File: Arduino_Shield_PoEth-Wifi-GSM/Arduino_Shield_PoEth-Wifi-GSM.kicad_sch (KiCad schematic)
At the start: 0 parts

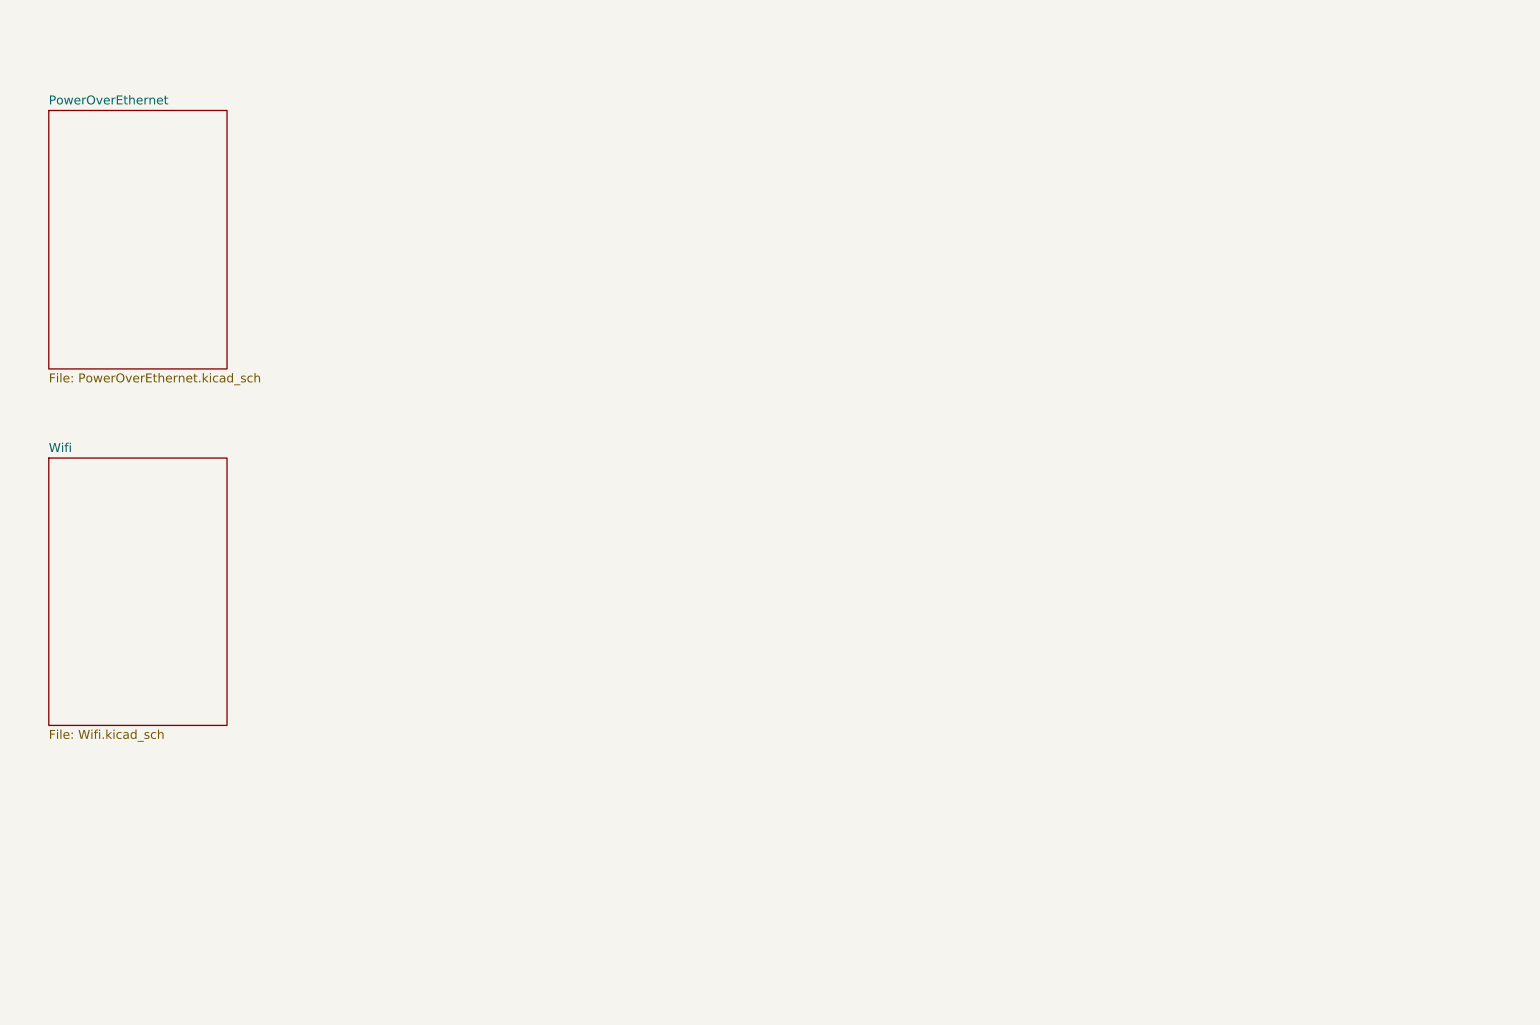
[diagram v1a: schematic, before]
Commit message: Tuning serial and crystal tracks
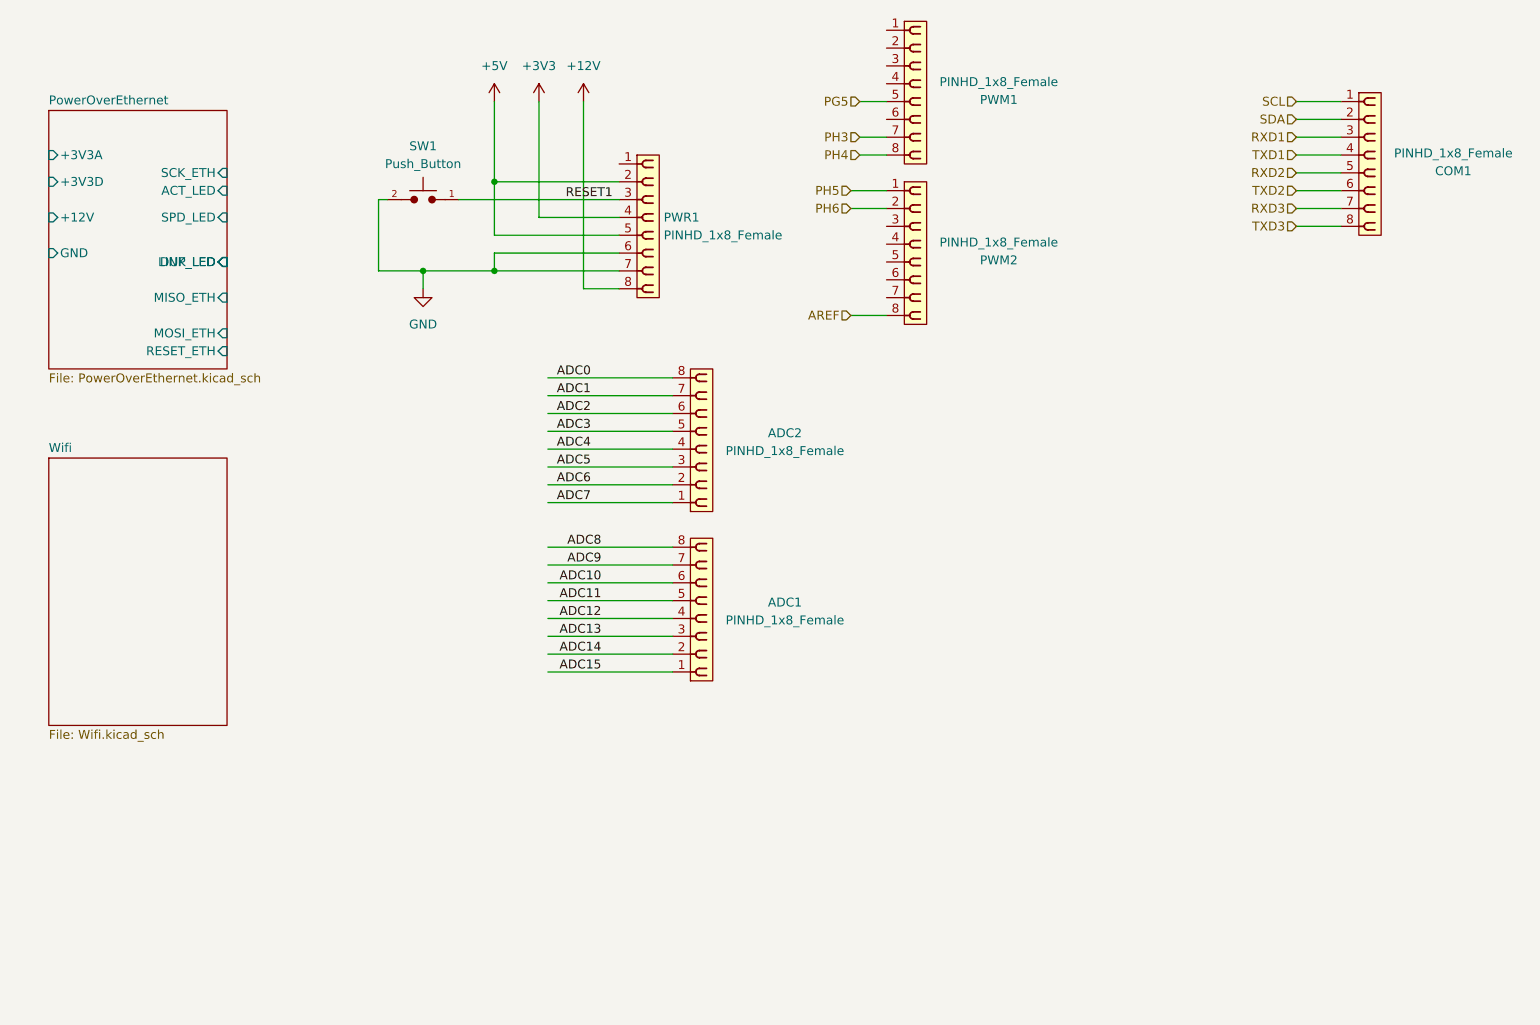
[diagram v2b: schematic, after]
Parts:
- added ADC1, ADC2, COM1, PWM1, PWM2, PWR1: PINHD_1x8_Female, Connector_PinSocket_2.54mm:PinSocket_1x08_P2.54mm_Vertical, symbol PCM_SL_Pin_Headers:PINHD_1x8_Female
- added SW1: Push_Button, Button_Switch_THT:SW_PUSH_6mm, symbol PCM_SL_Devices:Push_Button
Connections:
- new net +12V: PWR1.8
- new net +3V3: PWR1.4
- new net +5V: PWR1.2, PWR1.5
- new net ADC0: ADC2.8
- new net ADC1: ADC2.7
- new net ADC10: ADC1.6
- new net ADC11: ADC1.5
- new net ADC12: ADC1.4
- new net ADC13: ADC1.3
- new net ADC14: ADC1.2
- new net ADC15: ADC1.1
- new net ADC2: ADC2.6
- new net ADC3: ADC2.5
- new net ADC4: ADC2.4
- new net ADC5: ADC2.3
- new net ADC6: ADC2.2
- new net ADC7: ADC2.1
- new net ADC8: ADC1.8
- new net ADC9: ADC1.7
- new net AREF: PWM2.8
- new net GND: PWR1.6, PWR1.7, SW1.2
- new net PG5: PWM1.5
- new net PH3: PWM1.7
- new net PH4: PWM1.8
- new net PH5: PWM2.1
- new net PH6: PWM2.2
- new net RESET1: PWR1.3, SW1.1
- new net RXD1: COM1.3
- new net RXD2: COM1.5
- new net RXD3: COM1.7
- new net SCL: COM1.1
- new net SDA: COM1.2
- new net TXD1: COM1.4
- new net TXD2: COM1.6
- new net TXD3: COM1.8
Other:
- sheet PowerOverEthernet ports: added +12V, +3V3A, +3V3D, ACT_LED, DUP_LED, GND, LINK_LED, MISO_ETH, MOSI_ETH, RESET_ETH, SCK_ETH, SPD_LED; removed none

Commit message: Update Eth
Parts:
- added J1, J2: Conn_02x08, Connector_PinSocket_2.54mm:PinSocket_2x08_P2.54mm_Vertical, symbol PCM_4ms_Connector:Conn_02x08
- added J3, J4: PINHD_1x2_Female, Connector_PinSocket_2.54mm:PinSocket_1x02_P2.54mm_Vertical, symbol PCM_SL_Pin_Headers:PINHD_1x2_Female
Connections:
- net +5V: now also J3.1, J3.2
- net GND: now also J4.1, J4.2
- new net PA0: J2.16 (P16)
- new net PA1: J2.15 (-12V)
- new net PA2: J2.14 (-12V)
- new net PA3: J2.13 (-12)
- new net PA4: J2.12 (GND)
- new net PA5: J2.11 (GND)
- new net PA6: J2.10 (GND)
- new net PA7: J2.9 (GND)
- new net PB0: J1.1 (P1)
- new net PB1: J1.2 (P2)
- new net PB2: J1.3 (P3)
- new net PB3: J1.4 (P4)
- new net PC0: J2.1 (P1)
- new net PC1: J2.2 (P2)
- new net PC2: J2.3 (P3)
- new net PC3: J2.4 (P4)
- new net PC4: J2.5 (+12V)
- new net PC5: J2.6 (P6)
- new net PC6: J2.7 (12V)
- new net PC7: J2.8 (+12V)
- new net PD7: J1.16 (P16)
- new net PG0: J1.13 (-12)
- new net PG1: J1.14 (-12V)
- new net PG2: J1.15 (-12V)
- new net PL0: J1.5 (+12V)
- new net PL1: J1.6 (P6)
- new net PL2: J1.7 (12V)
- new net PL3: J1.8 (+12V)
- new net PL4: J1.9 (GND)
- new net PL5: J1.10 (GND)
- new net PL6: J1.11 (GND)
- new net PL7: J1.12 (GND)
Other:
- added sheet Power (arduinomega_power.kicad_sch)
